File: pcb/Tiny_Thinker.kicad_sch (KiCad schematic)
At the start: 50 parts, among them J2 PERIPHERALS, J3 ADC_TIM, J8 USB_C_Receptacle_USB2.0_16P, SW1 SW_Push, SW2 SW_SPDT, U1 STM32F446RET6, U2 AMS1117-3.3, U3 TPS2116DRL, Y1 16MHz

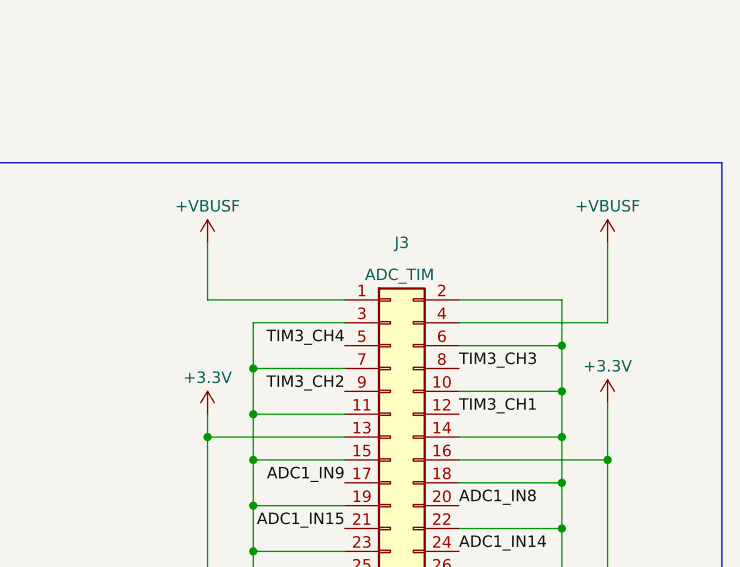
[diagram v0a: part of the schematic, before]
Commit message: broke out +5V external supply for expandability
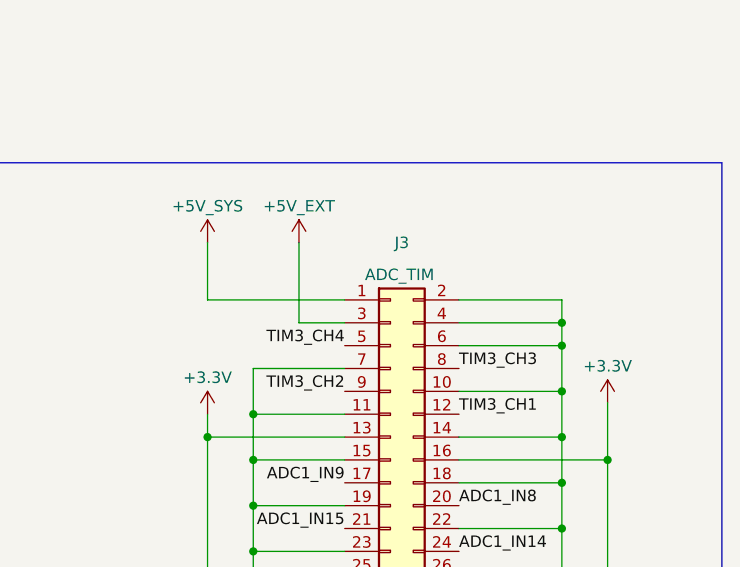
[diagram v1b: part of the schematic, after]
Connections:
- net +5V_EXT: now also J3.3 (Pin_3)
- net +5V_SYS: now also J3.1 (Pin_1)
- net +VBUSF: no longer J3.1 (Pin_1), J3.4 (Pin_4)
- net GND: now also J3.4 (Pin_4); no longer J3.3 (Pin_3)
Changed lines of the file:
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@@
 	)
 	(junction
-		(at 322.58 132.08)
+		(at 167.64 41.91)
 		(diameter 0)
 		(color 0 0 0 0)
 	)
 	(junction
-		(at 167.64 41.91)
+		(at 356.87 127)
 		(diameter 0)
 		(color 0 0 0 0)
@@
 	(wire
 		(pts
+			(xy 356.87 127) (xy 356.87 129.54)
+		)
+		(stroke
+			(width 0)
+			(type default)
+		)
+	)
+	(wire
+		(pts
 			(xy 104.14 182.88) (xy 110.49 182.88)
 		)
@@
 	(wire
 		(pts
-			(xy 322.58 127) (xy 322.58 132.08)
-		)
-		(stroke
-			(width 0)
-			(type default)
-		)
-	)
-	(wire
-		(pts
 			(xy 204.47 237.49) (xy 213.36 237.49)
 		)
@@
 	(wire
 		(pts
-			(xy 361.95 127) (xy 345.44 127)
-		)
-		(stroke
-			(width 0)
-			(type default)
-		)
-	)
-	(wire
-		(pts
 			(xy 120.65 120.65) (xy 143.51 120.65)
 		)
@@
 	(wire
 		(pts
+			(xy 345.44 127) (xy 356.87 127)
+		)
+		(stroke
+			(width 0)
+			(type default)
+		)
+	)
+	(wire
+		(pts
 			(xy 105.41 148.59) (xy 128.27 148.59)
 		)
@@
 	(wire
 		(pts
+			(xy 332.74 127) (xy 327.66 127)
+		)
+		(stroke
+			(width 0)
+			(type default)
+		)
+	)
+	(wire
+		(pts
 			(xy 226.06 40.64) (xy 232.41 40.64)
 		)
@@
 	(wire
 		(pts
-			(xy 356.87 124.46) (xy 356.87 129.54)
+			(xy 356.87 124.46) (xy 356.87 127)
 		)
 		(stroke
@@
 	(wire
 		(pts
-			(xy 361.95 118.11) (xy 361.95 127)
-		)
-		(stroke
-			(width 0)
-			(type default)
-		)
-	)
-	(wire
-		(pts
 			(xy 128.27 41.91) (xy 128.27 48.26)
 		)
@@
 	(wire
 		(pts
-			(xy 332.74 127) (xy 322.58 127)
-		)
-		(stroke
-			(width 0)
-			(type default)
-		)
-	)
-	(wire
-		(pts
 			(xy 143.51 116.84) (xy 143.51 120.65)
 		)
@@
 	(wire
 		(pts
+			(xy 327.66 127) (xy 327.66 118.11)
+		)
+		(stroke
+			(width 0)
+			(type default)
+		)
+	)
+	(wire
+		(pts
 			(xy 322.58 132.08) (xy 332.74 132.08)
 		)
@@
 	(symbol
 		(lib_id "power:VBUS")
-		(at 361.95 118.11 0)
-		(unit 1)
-		(exclude_from_sim no)
-		(in_bom yes)
-		(on_board yes)
-		(dnp no)
-		(property "Reference" "#PWR016"
-			(at 361.95 121.92 0)
-			(effects
-				(font
-					(size 1.27 1.27)
-				)
-				(hide yes)
-			)
-		)
-		(property "Value" "+VBUSF"
-			(at 361.95 114.046 0)
-			(effects
-				(font
-					(size 1.27 1.27)
-				)
-			)
-		)
-		(property "Footprint" ""
-			(at 361.95 118.11 0)
-			(effects
-				(font
-					(size 1.27 1.27)
-				)
-				(hide yes)
-			)
-		)
-		(property "Datasheet" ""
-			(at 361.95 118.11 0)
-			(effects
-				(font
-					(size 1.27 1.27)
-				)
-				(hide yes)
-			)
-		)
-		(property "Description" "Power symbol creates a global label with name \"VBUS\""
-			(at 361.95 118.11 0)
-			(effects
-				(font
-					(size 1.27 1.27)
-				)
-				(hide yes)
-			)
-		)
-		(pin "1"
-		)
-		(instances
-			(project "Tiny_Thinker"
-				(path "/1492d82e-cea7-4984-859f-7eb0a1e67ad8"
-					(reference "#PWR016")
-					(unit 1)
-				)
-			)
-		)
-	)
-	(symbol
-		(lib_id "power:VBUS")
 		(at 218.44 237.49 0)
 		(unit 1)
@@
 			)
 		)
-		(property "Value" "+VBUSF"
+		(property "Value" "+5V_SYS"
 			(at 317.5 114.046 0)
 			(effects
@@
 					(unit 1)
 				)
+			)
+		)
+	)
+	(symbol
+		(lib_id "power:VBUS")
+		(at 327.66 118.11 0)
+		(unit 1)
+		(exclude_from_sim no)
+		(in_bom yes)
+		(on_board yes)
+		(dnp no)
+		(property "Reference" "#PWR032"
+			(at 327.66 121.92 0)
+			(effects
+				(font
+					(size 1.27 1.27)
+				)
+				(hide yes)
+			)
+		)
+		(property "Value" "+5V_EXT"
+			(at 327.66 114.046 0)
+			(effects
+				(font
+					(size 1.27 1.27)
+				)
+			)
+		)
+		(property "Footprint" ""
+			(at 327.66 118.11 0)
+			(effects
+				(font
+					(size 1.27 1.27)
+				)
+				(hide yes)
+			)
+		)
+		(property "Datasheet" ""
+			(at 327.66 118.11 0)
+			(effects
+				(font
+					(size 1.27 1.27)
+				)
+				(hide yes)
+			)
+		)
+		(property "Description" "Power symbol creates a global label with name \"VBUS\""
+			(at 327.66 118.11 0)
+			(effects
+				(font
+					(size 1.27 1.27)
+				)
+				(hide yes)
+			)
+		)
+		(pin "1"
+		)
+		(instances
+			(project "Tiny_Thinker"
+				(path "/1492d82e-cea7-4984-859f-7eb0a1e67ad8"
+					(reference "#PWR032")
+					(unit 1)
+				)

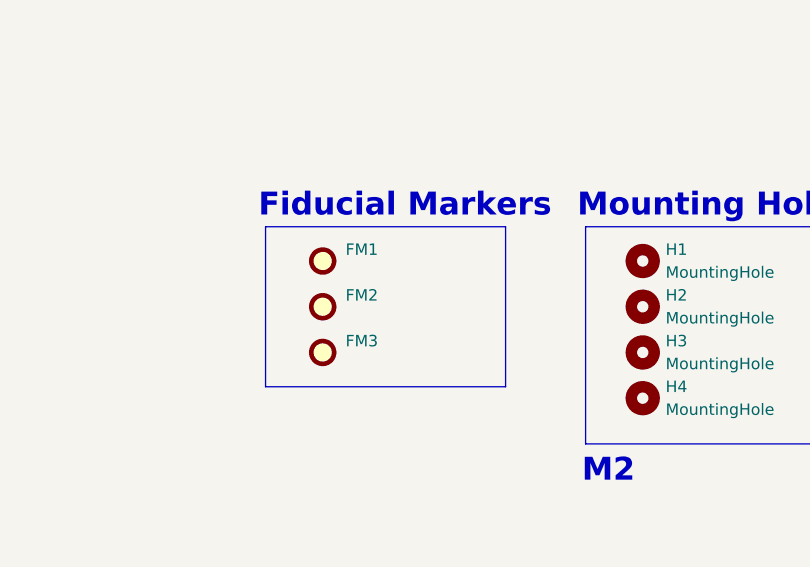
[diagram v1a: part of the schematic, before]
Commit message: changed 10k Ohm resistor JLCPCB part and removed fiducial markers (jlc does it for you)
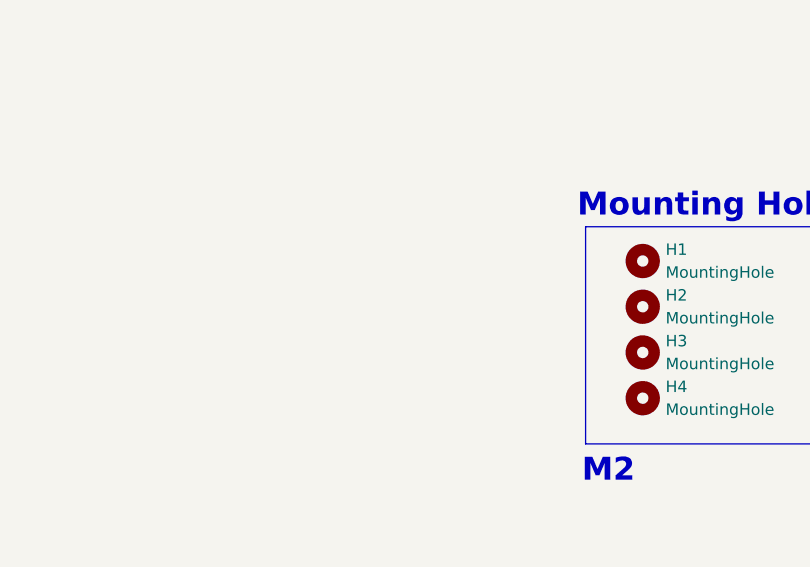
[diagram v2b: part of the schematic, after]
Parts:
- removed FM1, FM2, FM3: Fiducial, Fiducial:Fiducial_1mm_Mask2mm, symbol Mechanical:Fiducial
- R1, R4: JLCPCB Part # C25531 -> C25744
- U3: JLCPCB Part # (none) -> C3235557
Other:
- note removed: "Fiducial Markers"
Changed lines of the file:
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@@
 	)
 	(rectangle
-		(start 43.18 48.26)
-		(end 69.85 66.04)
-		(stroke
-			(width 0)
-			(type default)
-		)
-		(fill
-			(type none)
-		)
-	)
-	(rectangle
 		(start 241.3 109.22)
 		(end 374.65 186.69)
@@
 		)
 	)
-	(text "Fiducial Markers\n"
-		(exclude_from_sim no)
-		(at 58.674 45.974 0)
-		(effects
-			(font
-				(size 2.54 2.54)
-				(thickness 0.508)
-				(bold yes)
-			)
-		)
-	)
 	(text "Header Pins"
 		(exclude_from_sim no)
@@
 			)
 		)
-		(property "JLCPCB Part #" "C25531"
+		(property "JLCPCB Part #" "C25744"
 			(at 93.98 172.72 90)
 			(effects
@@
 			)
 		)
-		(property "JLCPCB Part #" "C25531"
+		(property "JLCPCB Part #" "C25744"
 			(at 198.12 171.45 0)
 			(effects
@@
 	)
 	(symbol
-		(lib_id "Mechanical:Fiducial")
-		(at 49.53 52.07 0)
-		(unit 1)
-		(exclude_from_sim no)
-		(in_bom no)
-		(on_board yes)
-		(dnp no)
-		(fields_autoplaced yes)
-		(property "Reference" "FM1"
-			(at 52.07 50.7999 0)
-			(effects
-				(font
-					(size 1.27 1.27)
-				)
-				(justify left)
-			)
-		)
-		(property "Value" "Fiducial"
-			(at 52.07 53.3399 0)
-			(effects
-				(font
-					(size 1.27 1.27)
-				)
-				(justify left)
-				(hide yes)
-			)
-		)
-		(property "Footprint" "Fiducial:Fiducial_1mm_Mask2mm"
-			(at 49.53 52.07 0)
-			(effects
-				(font
-					(size 1.27 1.27)
-				)
-				(hide yes)
-			)
-		)
-		(property "Datasheet" "~"
-			(at 49.53 52.07 0)
-			(effects
-				(font
-					(size 1.27 1.27)
-				)
-				(hide yes)
-			)
-		)
-		(property "Description" "Fiducial Marker"
-			(at 49.53 52.07 0)
-			(effects
-				(font
-					(size 1.27 1.27)
-				)
-				(hide yes)
-			)
-		)
-		(instances
-			(project ""
-				(path "/1492d82e-cea7-4984-859f-7eb0a1e67ad8"
-					(reference "FM1")
-					(unit 1)
-				)
-			)
-		)
-	)
-	(symbol
 		(lib_id "Device:LED")
 		(at 179.07 36.83 180)
@@
 			)
 		)
+		(property "JLCPCB Part #" "C3235557"
+			(at 240.03 233.68 0)
+			(effects
+				(font
+					(size 1.27 1.27)
+				)
+				(hide yes)
+			)
+		)
 		(pin "4"
 		)
@@
 	)
 	(symbol
-		(lib_id "Mechanical:Fiducial")
-		(at 49.53 62.23 0)
-		(unit 1)
-		(exclude_from_sim no)
-		(in_bom no)
-		(on_board yes)
-		(dnp no)
-		(fields_autoplaced yes)
-		(property "Reference" "FM3"
-			(at 52.07 60.9599 0)
-			(effects
-				(font
-					(size 1.27 1.27)
-				)
-				(justify left)
-			)
-		)
-		(property "Value" "Fiducial"
-			(at 52.07 63.4999 0)
-			(effects
-				(font
-					(size 1.27 1.27)
-				)
-				(justify left)
-				(hide yes)
-			)
-		)
-		(property "Footprint" "Fiducial:Fiducial_1mm_Mask2mm"
-			(at 49.53 62.23 0)
-			(effects
-				(font
-					(size 1.27 1.27)
-				)
-				(hide yes)
-			)
-		)
-		(property "Datasheet" "~"
-			(at 49.53 62.23 0)
-			(effects
-				(font
-					(size 1.27 1.27)
-				)
-				(hide yes)
-			)
-		)
-		(property "Description" "Fiducial Marker"
-			(at 49.53 62.23 0)
-			(effects
-				(font
-					(size 1.27 1.27)
-				)
-				(hide yes)
-			)
-		)
-		(instances
-			(project "Tiny_Thinker"
-				(path "/1492d82e-cea7-4984-859f-7eb0a1e67ad8"
-					(reference "FM3")
-					(unit 1)
-				)
-			)
-		)
-	)
-	(symbol
 		(lib_id "power:GND")
 		(at 74.93 157.48 0)
@@
 					(unit 1)
 				)
-			)
-		)
-	)
-	(symbol
-		(lib_id "Mechanical:Fiducial")
-		(at 49.53 57.15 0)
-		(unit 1)
-		(exclude_from_sim no)
-		(in_bom no)
-		(on_board yes)
-		(dnp no)
-		(fields_autoplaced yes)
-		(property "Reference" "FM2"
-			(at 52.07 55.8799 0)
-			(effects
-				(font
-					(size 1.27 1.27)
-				)
-				(justify left)
-			)
-		)
-		(property "Value" "Fiducial"
-			(at 52.07 58.4199 0)
-			(effects
-				(font
-					(size 1.27 1.27)
-				)
-				(justify left)
-				(hide yes)
-			)
-		)
-		(property "Footprint" "Fiducial:Fiducial_1mm_Mask2mm"
-			(at 49.53 57.15 0)
-			(effects
-				(font
-					(size 1.27 1.27)
-				)
-				(hide yes)
-			)
-		)
-		(property "Datasheet" "~"
-			(at 49.53 57.15 0)
-			(effects
-				(font
-					(size 1.27 1.27)
-				)
-				(hide yes)
-			)
-		)
-		(property "Description" "Fiducial Marker"
-			(at 49.53 57.15 0)
-			(effects
-				(font
-					(size 1.27 1.27)
-				)
-				(hide yes)
-			)
-		)
-		(instances
-			(project "Tiny_Thinker"
-				(path "/1492d82e-cea7-4984-859f-7eb0a1e67ad8"
-					(reference "FM2")
-					(unit 1)
-				)

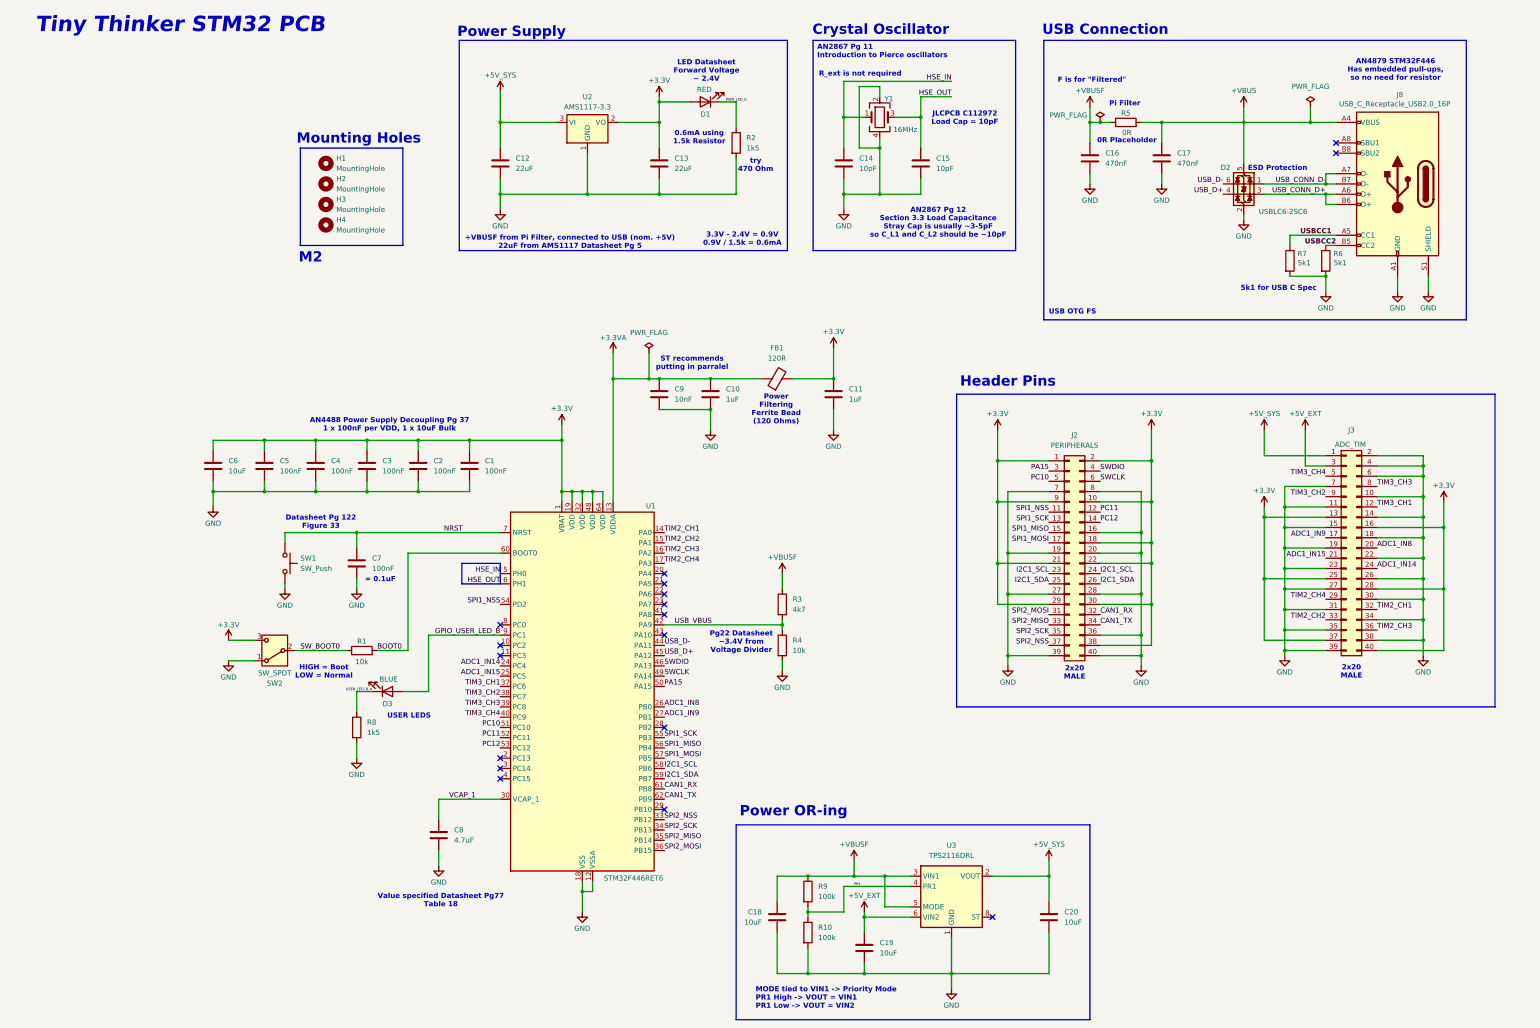
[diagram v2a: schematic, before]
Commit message: added stitching vias and cleaned up silkscreen
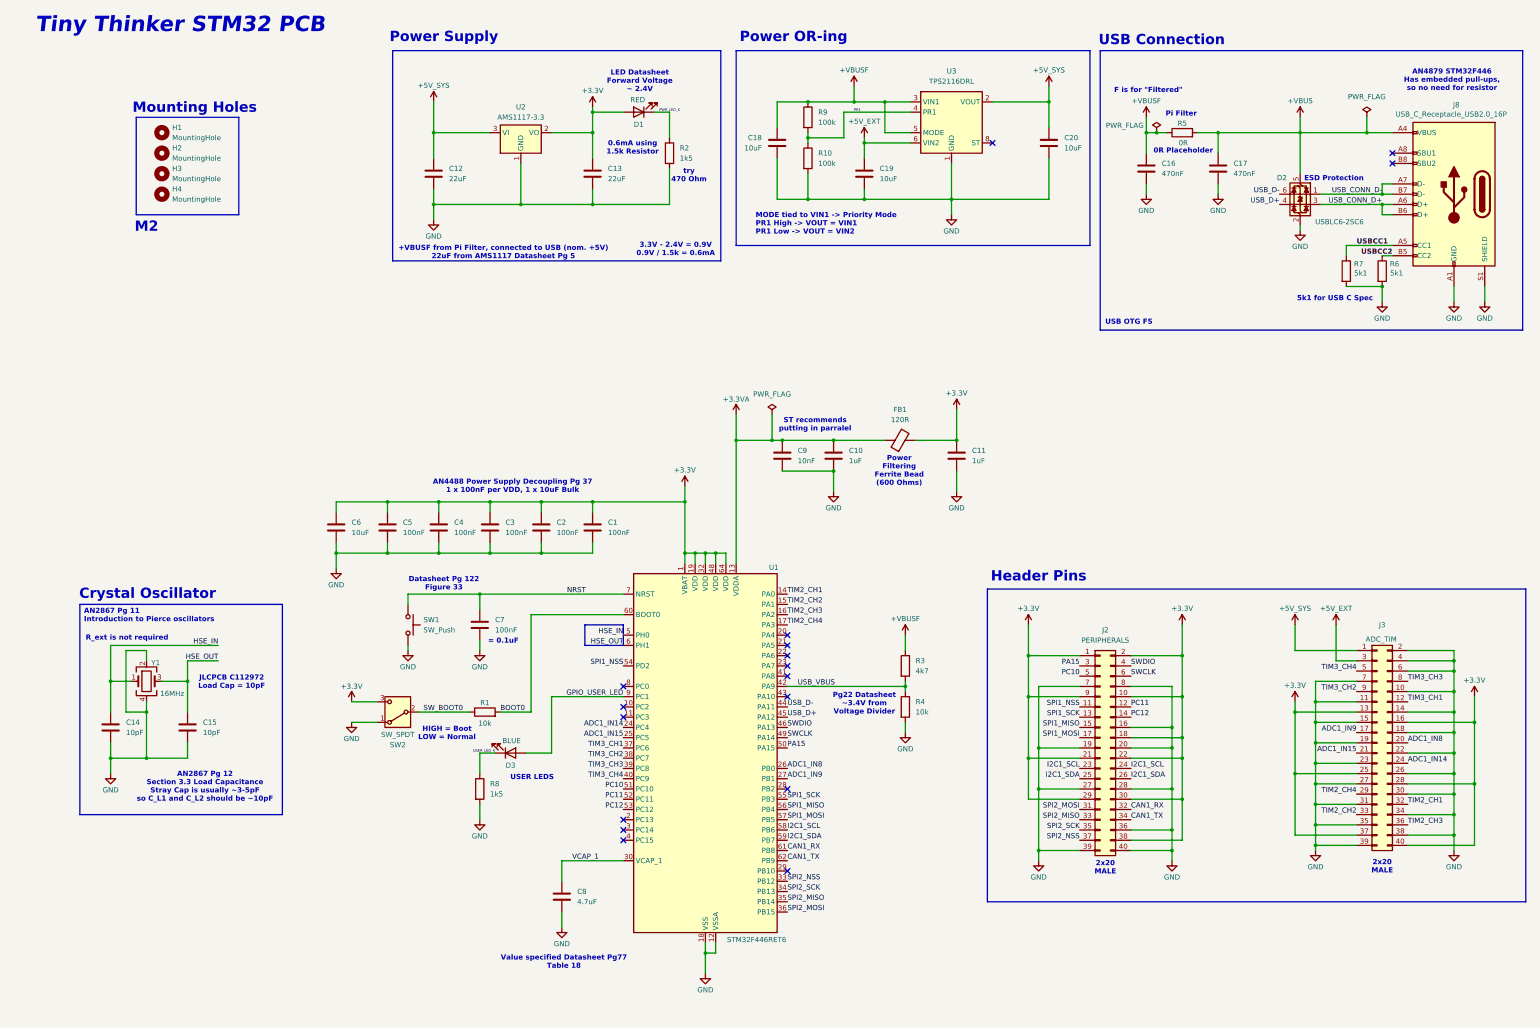
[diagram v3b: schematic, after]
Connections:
- net GPIO_USER_LED_B renamed GPIO_USER_LED
- net USER_LED_B_K renamed USER_LED_K
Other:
- note added: "Power Filtering Ferrite Bead (600 Ohms)"
- note removed: "Power Filtering Ferrite Bead (120 Ohms)"
- moved on the sheet: C1, C10, C11, C12, C13, C14, C15, C16, C17, C18, C19, C2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
